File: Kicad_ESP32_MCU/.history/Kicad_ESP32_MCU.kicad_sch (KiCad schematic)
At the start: 1 part, among them U1 ESP32-S3-WROOM-1

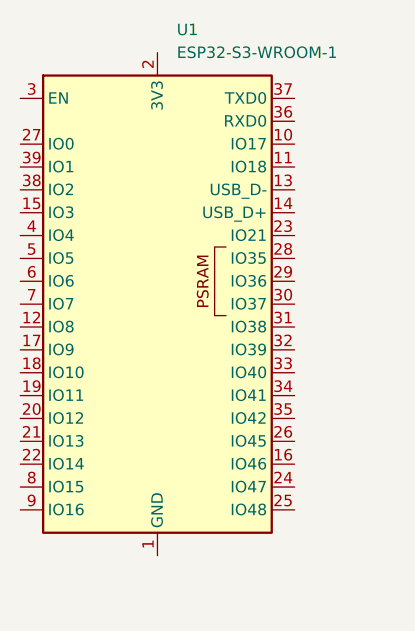
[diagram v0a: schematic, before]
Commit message: Finish uart_comm.cpp/h
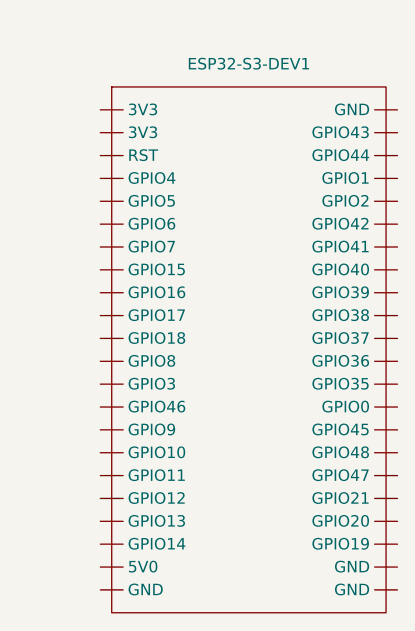
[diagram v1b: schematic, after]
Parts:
- removed U1: ESP32-S3-WROOM-1, RF_Module:ESP32-S3-WROOM-1, symbol RF_Module:ESP32-S3-WROOM-1
- added ESP32-S3-DEV1: (no value), symbol ESP32_S3_DEV:board
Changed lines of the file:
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@@
 	(paper "A4")
 	(symbol
-		(lib_id "RF_Module:ESP32-S3-WROOM-1")
-		(at 134.62 85.09 0)
+		(lib_id "ESP32_S3_DEV:board")
+		(at 144.78 63.5 0)
 		(unit 1)
 		(body_style 1)
@@
 		(dnp no)
 		(fields_autoplaced yes)
-		(property "Reference" "U1"
-			(at 136.7633 54.61 0)
+		(property "Reference" "ESP32-S3-DEV1"
+			(at 144.78 58.42 0)
 			(show_name no)
 			(do_not_autoplace no)
@@
 					(size 1.27 1.27)
 				)
-				(justify left)
 			)
 		)
-		(property "Value" "ESP32-S3-WROOM-1"
-			(at 136.7633 57.15 0)
+		(property "Value" ""
+			(at 144.78 63.5 0)
 			(show_name no)
 			(do_not_autoplace no)
@@
 					(size 1.27 1.27)
 				)
-				(justify left)
 			)
 		)
-		(property "Footprint" "RF_Module:ESP32-S3-WROOM-1"
-			(at 134.62 82.55 0)
+		(property "Footprint" ""
+			(at 144.78 63.5 0)
 			(hide yes)
 			(show_name no)
@@
 			)
 		)
-		(property "Datasheet" "https://www.espressif.com/sites/default/files/documentation/esp32-s3-wroom-1_wroom-1u_datasheet_en.pdf"
-			(at 134.62 85.09 0)
+		(property "Datasheet" ""
+			(at 144.78 63.5 0)
 			(hide yes)
 			(show_name no)
@@
 			)
 		)
-		(property "Description" "RF Module, ESP32-S3 SoC, Wi-Fi 802.11b/g/n, Bluetooth, BLE, 32-bit, 3.3V, onboard antenna, SMD"
-			(at 134.62 85.09 0)
+		(property "Description" ""
+			(at 144.78 63.5 0)
 			(hide yes)
 			(show_name no)
@@
 			)
 		)
-		(pin "6"
+		(pin ""
 		)
-		(pin "23"
+		(pin ""
 		)
-		(pin "25"
+		(pin ""
 		)
-		(pin "27"
+		(pin ""
 		)
-		(pin "1"
+		(pin ""
 		)
-		(pin "11"
+		(pin ""
 		)
-		(pin "2"
+		(pin ""
 		)
-		(pin "7"
+		(pin ""
 		)
-		(pin "9"
+		(pin ""
 		)
-		(pin "8"
+		(pin ""
 		)
-		(pin "5"
+		(pin ""
 		)
-		(pin "10"
+		(pin ""
 		)
-		(pin "12"
+		(pin ""
 		)
-		(pin "3"
+		(pin ""
 		)
-		(pin "13"
+		(pin ""
 		)
-		(pin "14"
+		(pin ""
 		)
-		(pin "15"
+		(pin ""
 		)
-		(pin "16"
+		(pin ""
 		)
-		(pin "18"
+		(pin ""
 		)
-		(pin "17"
+		(pin ""
 		)
-		(pin "19"
+		(pin ""
 		)
-		(pin "20"
+		(pin ""
 		)
-		(pin "4"
+		(pin ""
 		)
-		(pin "21"
+		(pin ""
 		)
-		(pin "22"
+		(pin ""
 		)
-		(pin "24"
+		(pin ""
 		)
-		(pin "26"
+		(pin ""
 		)
-		(pin "37"
+		(pin ""
 		)
-		(pin "40"
+		(pin ""
 		)
-		(pin "29"
+		(pin ""
 		)
-		(pin "32"
+		(pin ""
 		)
-		(pin "39"
+		(pin ""
 		)
-		(pin "33"
+		(pin ""
 		)
-		(pin "35"
+		(pin ""
 		)
-		(pin "38"
+		(pin ""
 		)
-		(pin "31"
+		(pin ""
 		)
-		(pin "34"
+		(pin ""
 		)
-		(pin "28"
+		(pin ""
 		)
-		(pin "30"
+		(pin ""
 		)
-		(pin "36"
+		(pin ""
 		)
-		(pin "41"
+		(pin ""
+		)
+		(pin ""
+		)
+		(pin ""
+		)
+		(pin ""
 		)
 		(instances
 			(project "Kicad_ESP32_MCU"
 				(path "/de6a28c1-3142-4bac-853f-bf312f7edabc"
-					(reference "U1")
+					(reference "ESP32-S3-DEV1")
 					(unit 1)
 				)
